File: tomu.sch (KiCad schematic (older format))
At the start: 15 parts, among them P1 USART0, P2 DEBUG, P3 USB_PCB, U1 EFM32HG309

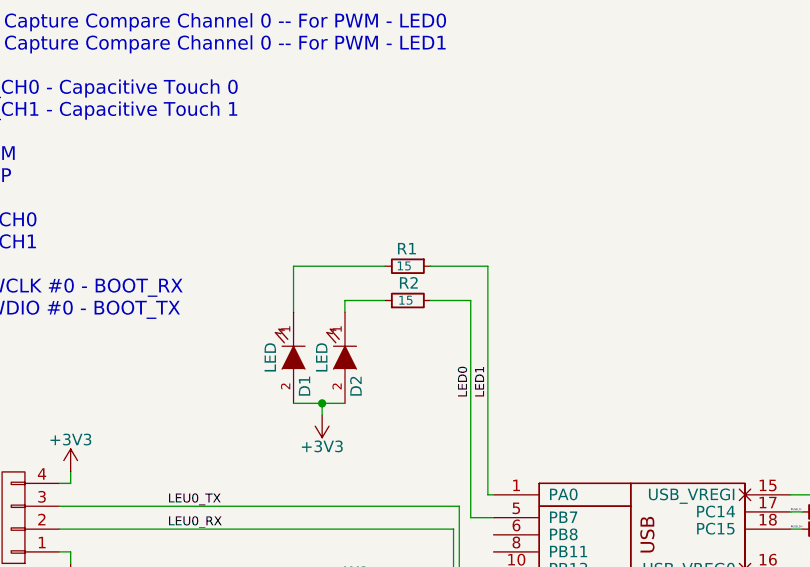
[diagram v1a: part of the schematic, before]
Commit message: Update value of diode resistors.
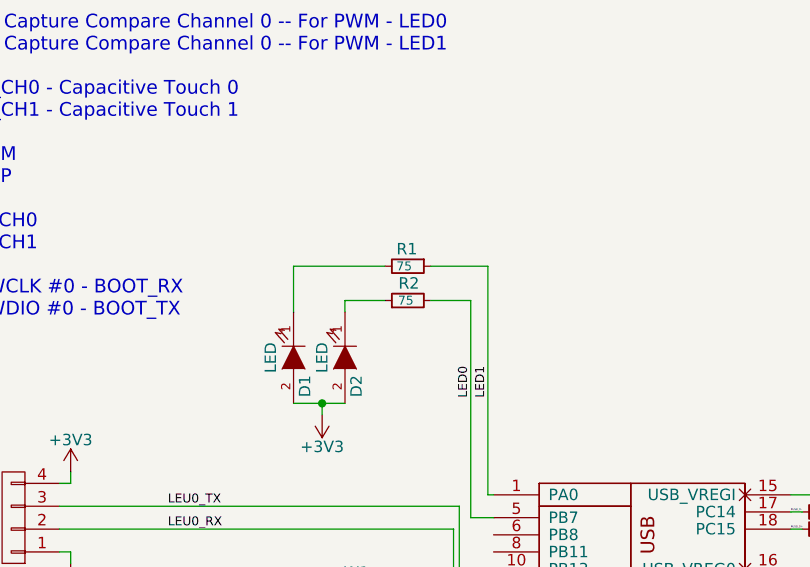
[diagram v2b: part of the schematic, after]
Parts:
- R1, R2: value 15 -> 75
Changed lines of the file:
@@
 P 3825 2175
 F 0 "R2" V 3900 2125 50  0000 L CNN
-F 1 "15" V 3825 2150 39  0000 L CNN
+F 1 "75" V 3825 2150 39  0000 L CNN
 F 2 "Resistors_SMD:R_0402" H 3825 2175 50  0001 C CNN
 F 3 "" H 3825 2175 50  0000 C CNN
@@
 P 3825 2025
 F 0 "R1" V 3750 1975 50  0000 L CNN
-F 1 "15" V 3825 1975 39  0000 L CNN
+F 1 "75" V 3825 1975 39  0000 L CNN
 F 2 "Resistors_SMD:R_0402" H 3825 2025 50  0001 C CNN
 F 3 "" H 3825 2025 50  0000 C CNN

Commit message: s/usb_pcb/usb-pcb/ s/USB_PCB/USB-PCB/
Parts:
- P3: value USB_PCB -> USB-PCB; symbol USB_PCB -> USB-PCB
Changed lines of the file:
@@
 LIBS:valves
 LIBS:efm32hg309
-LIBS:usb_pcb
+LIBS:usb-pcb
 LIBS:tomu-cache
 EELAYER 25 0
@@
 $EndComp
 $Comp
-L USB_PCB P3
+L USB-PCB P3
 U 1 1 5798BECB
 P 6650 3225
 F 0 "P3" H 6850 3025 50  0000 C CNN
-F 1 "USB_PCB" H 6600 3425 50  0000 C CNN
+F 1 "USB-PCB" H 6600 3425 50  0000 C CNN
 F 2 "usb-pcb:USB-PCB" V 6600 3125 50  0001 C CNN
 F 3 "" V 6600 3125 50  0000 C CNN
